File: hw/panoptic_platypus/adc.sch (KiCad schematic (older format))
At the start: 33 parts

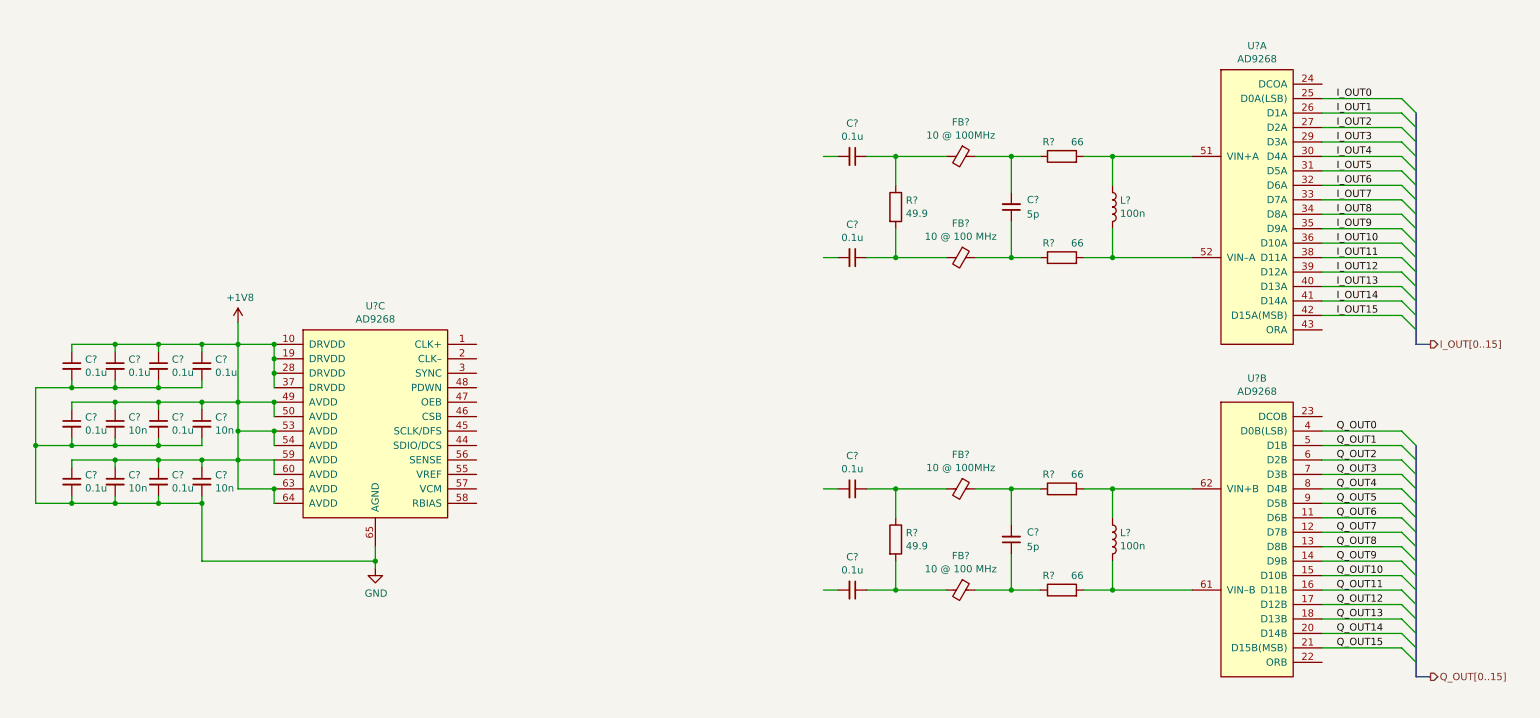
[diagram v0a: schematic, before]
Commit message: adc stage shematic finished
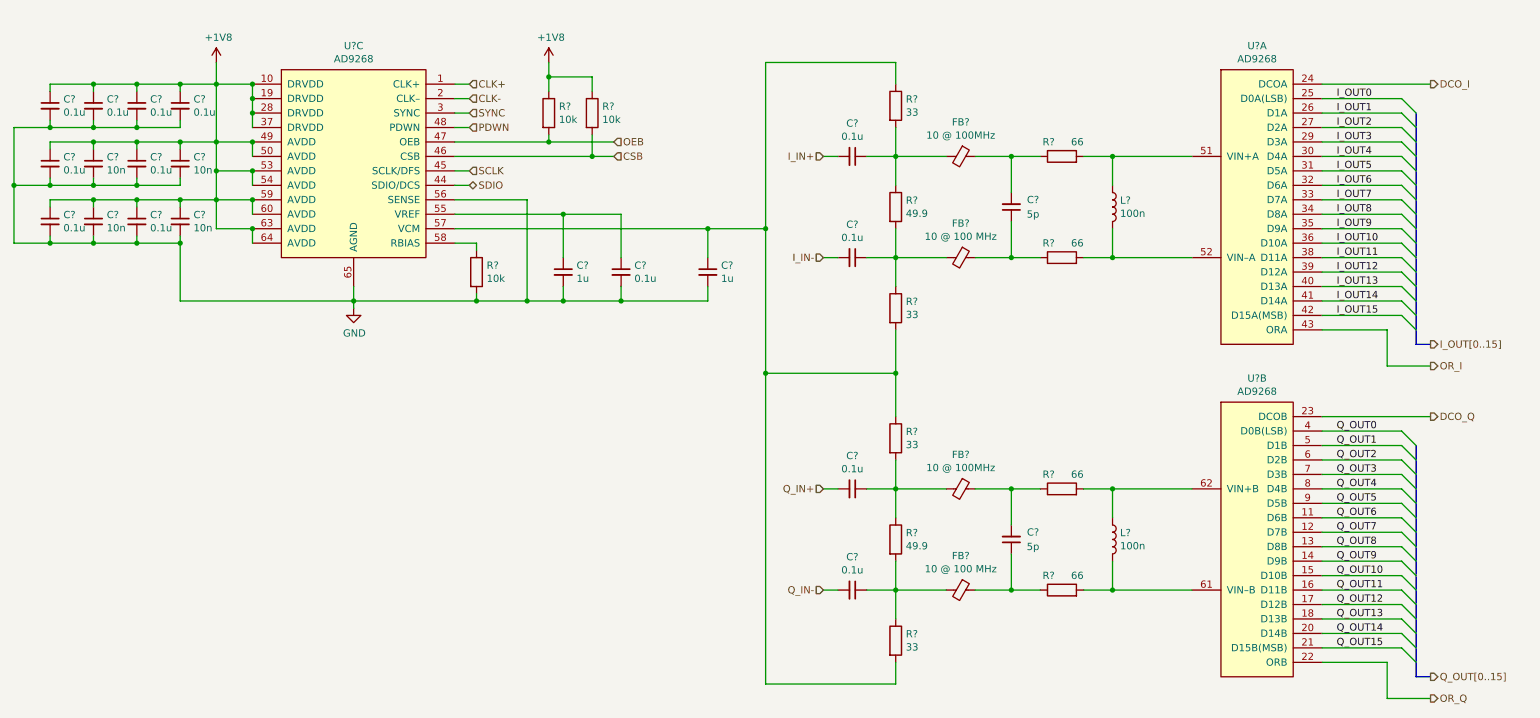
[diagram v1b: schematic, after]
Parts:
- added C? (x2): 1u, symbol Device:C_Small
- added C?: 0.1u, symbol Device:C_Small
- added R? (x3): 10k, symbol Device:R
- added R? (x4): 33, symbol Device:R
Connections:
- net labels added: CLK+, CLK-, CSB, DCO_I, DCO_Q, I_IN+, I_IN-, OEB, OR_I, OR_Q, PDWN, Q_IN+, Q_IN-, SCLK, SDIO, SYNC
- wire segments 143 -> 201
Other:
- moved on the sheet: C?, U?C

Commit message: updated some symbols added some ICs
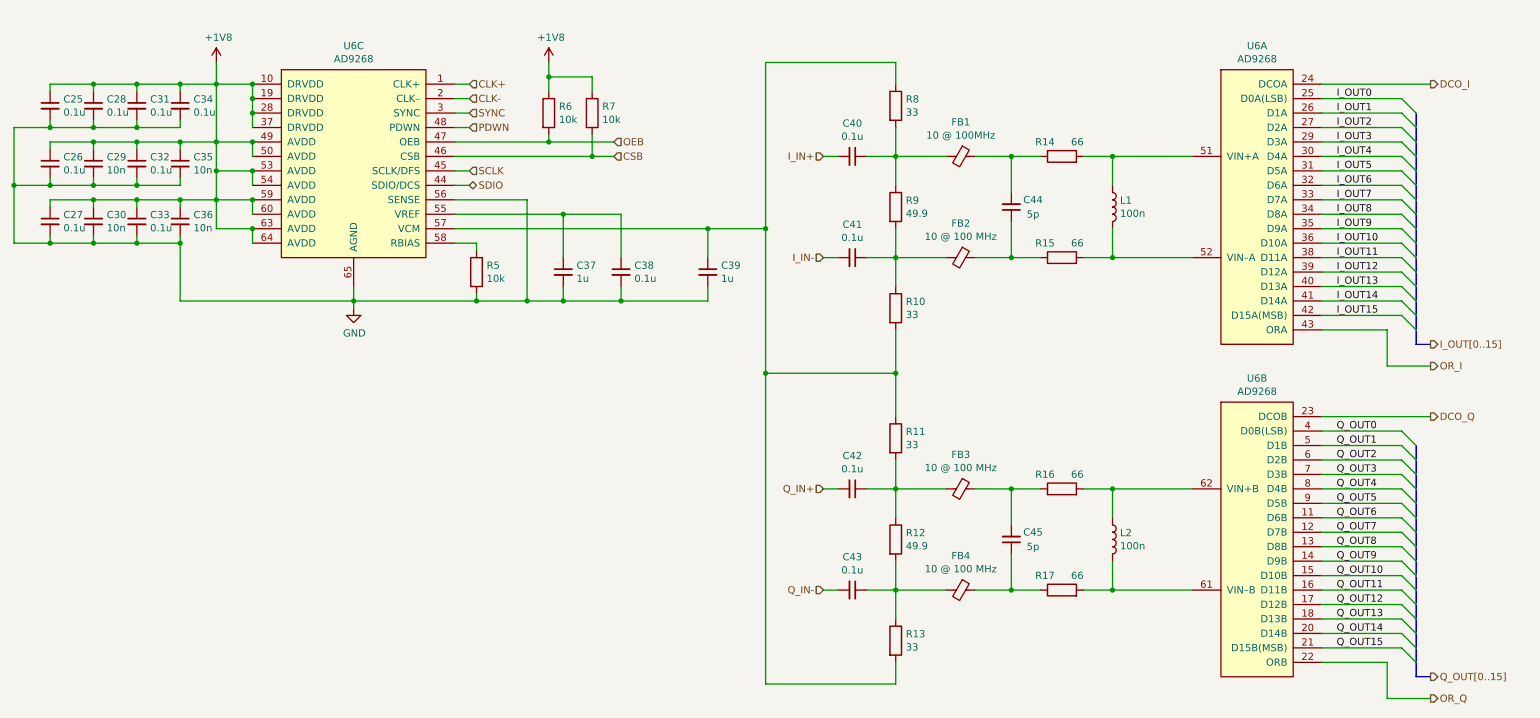
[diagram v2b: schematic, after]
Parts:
- C25, C26, C27, C28, C29, C30, C31, C32, C33, C34, C35, C36, C37, C38, C39, C40, C41, C42, C43, C44, C45: renamed from C?; footprint (none) -> Capacitor_SMD:C_0402_1005Metric
- FB1, FB2, FB4: renamed from FB?; footprint (none) -> Capacitor_SMD:C_0402_1005Metric
- FB3: renamed from FB?; value 10 @ 100MHz -> 10 @ 100 MHz; footprint (none) -> Capacitor_SMD:C_0402_1005Metric
- L1, L2: renamed from L?; footprint (none) -> Inductor_SMD:L_0402_1005Metric
- R10, R11, R12, R13, R14, R15, R16, R17, R5, R6, R7, R8, R9: renamed from R?; footprint (none) -> Resistor_SMD:R_0402_1005Metric
- gave numbers to parts that had none: 1

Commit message: Added LO Generator, fixed some smybols
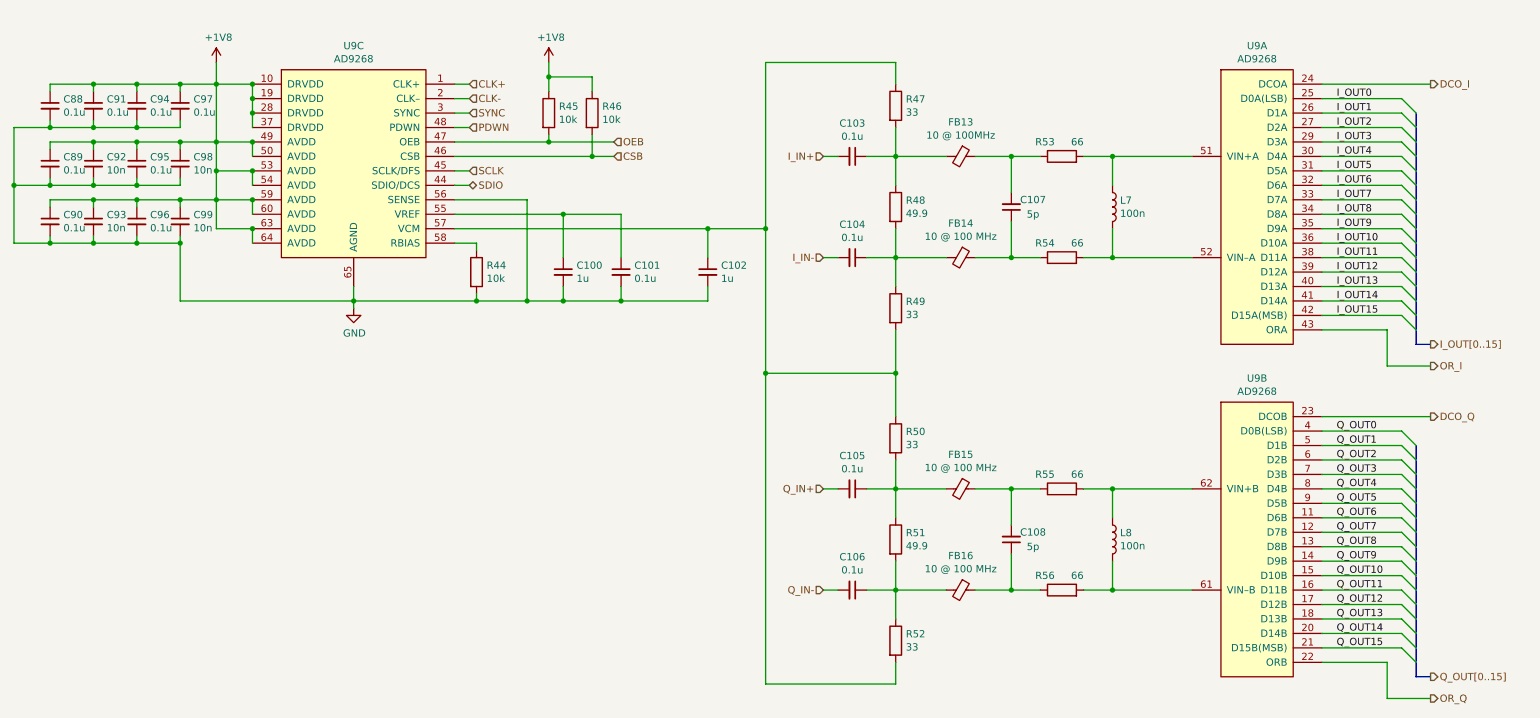
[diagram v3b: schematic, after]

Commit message: updated power scheme
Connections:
- net +1V8 renamed AVDD
- net AVDD: no longer C25.1, C28.1, C31.1, C34.1, R6.1, R7.1, U6.10 (DRVDD), U6.19 (DRVDD), U6.28 (DRVDD), U6.37 (DRVDD)
- new net DRVDD: C25.1, C28.1, C31.1, C34.1, R6.1, R7.1, U6.10 (DRVDD), U6.19 (DRVDD), U6.28 (DRVDD), U6.37 (DRVDD)
